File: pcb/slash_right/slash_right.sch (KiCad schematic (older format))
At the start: 138 parts, among them J1 RJ12, J2 AVR-ISP-6, J3 USB_B_Mini, SW1 SW_Push, SW10 SW_Push_45deg, SW11 SW_Push_45deg, SW12 SW_Push_45deg, SW13 SW_Push_45deg, SW14 SW_Push_45deg, SW15 SW_Push_45deg, SW16 SW_Push_45deg, SW17 SW_Push_45deg, SW18 SW_Push_45deg, SW19 SW_Push_45deg, SW2 SW_Push_45deg, SW20 SW_Push_45deg, SW21 SW_Push_45deg, SW22 SW_Push_45deg, SW23 SW_Push_45deg, SW24 SW_Push_45deg, SW25 SW_Push_45deg, SW26 SW_Push_45deg, SW27 SW_Push_45deg, SW28 SW_Push_45deg, SW29 SW_Push_45deg, SW3 SW_Push_45deg, SW30 SW_Push_45deg, SW31 SW_Push_45deg, SW32 SW_Push_45deg, SW33 SW_Push_45deg, SW34 SW_Push_45deg, SW35 SW_Push_45deg, SW36 SW_Push_45deg, SW37 SW_Push_45deg, SW38 SW_Push_45deg, SW39 SW_Push_45deg, SW4 SW_Push_45deg, SW40 SW_Push_45deg, SW41 SW_Push_45deg, SW42 SW_Push_45deg, SW43 SW_Push_45deg, SW44 SW_Push_45deg, SW45 SW_Push_45deg, SW46 SW_Push_45deg, SW47 SW_Push_45deg, SW48 SW_Push_45deg, SW49 SW_Push_45deg, SW5 SW_Push_45deg, SW50 SW_Push_45deg, SW51 SW_Push_45deg, SW52 SW_Push_45deg, SW53 SW_Push_45deg, SW54 SW_Push_45deg, SW55 SW_Push_45deg, SW56 SW_Push_45deg, SW6 SW_Push_45deg, SW7 SW_Push_45deg, SW8 SW_Push_45deg, SW9 SW_Push_45deg, U1 ATmega32U4-AU, Y1 16MHz

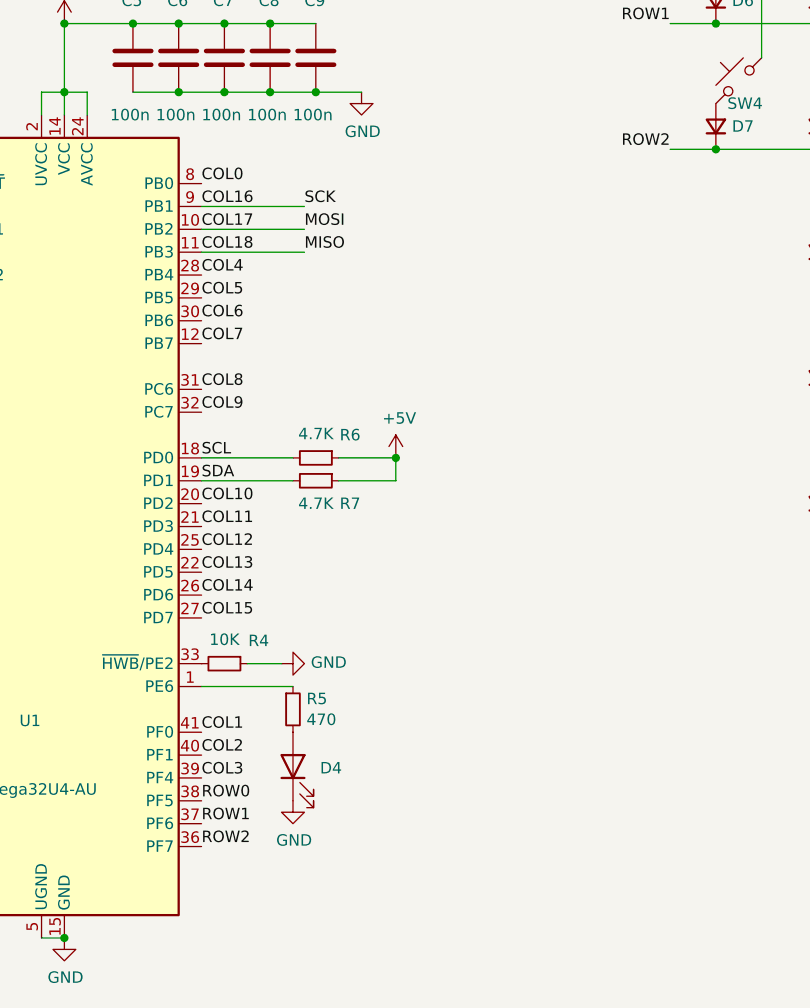
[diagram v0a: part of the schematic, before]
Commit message: pcb: slash: more routing
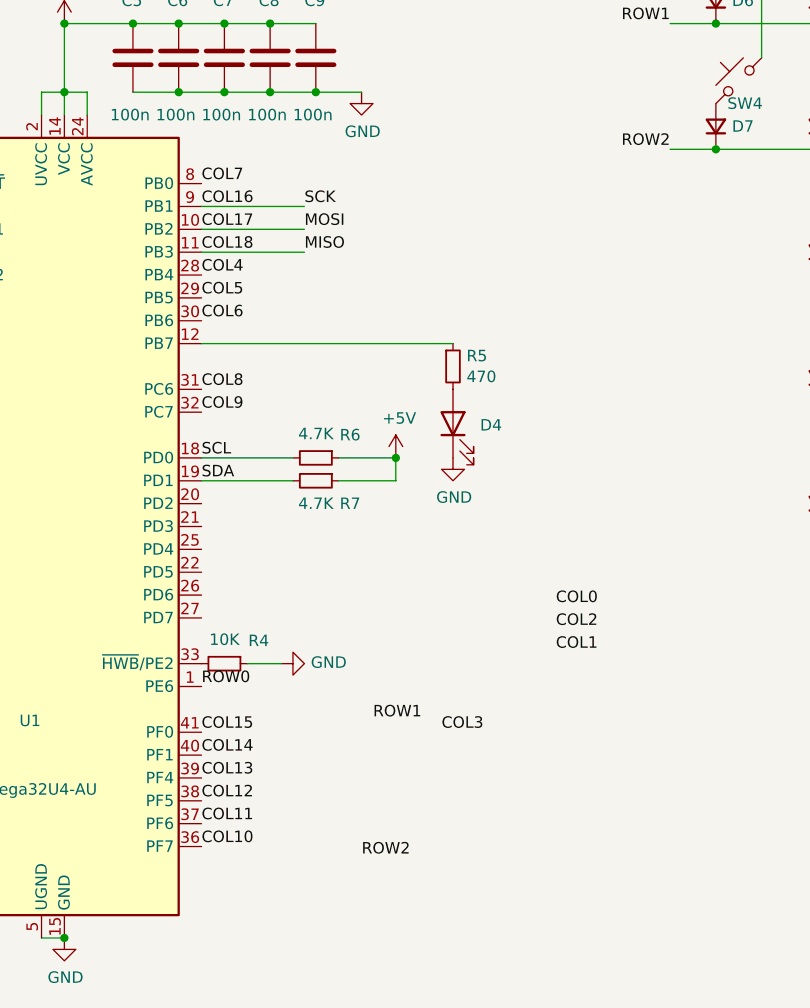
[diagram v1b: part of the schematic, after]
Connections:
- net COL0: no longer U1.8 (PB0)
- net COL1: no longer U1.41 (PF0)
- net COL10: now also U1.36 (PF7); no longer U1.20 (PD2)
- net COL11: now also U1.37 (PF6); no longer U1.21 (PD3)
- net COL12: now also U1.38 (PF5); no longer U1.25 (PD4)
- net COL13: now also U1.39 (PF4); no longer U1.22 (PD5)
- net COL14: now also U1.40 (PF1); no longer U1.26 (PD6)
- net COL15: now also U1.41 (PF0); no longer U1.27 (PD7)
- net COL2: no longer U1.40 (PF1)
- net COL3: no longer U1.39 (PF4)
- net COL7: now also U1.8 (PB0); no longer U1.12 (PB7)
- net ROW0: now also U1.1 (PE6); no longer U1.38 (PF5)
- net ROW1: no longer U1.37 (PF6)
- net ROW2: no longer U1.36 (PF7)
- net at R5.1: now also U1.12 (PB7); no longer U1.1 (PE6)
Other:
- moved on the sheet: D4, R5
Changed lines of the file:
@@
 Text Label 1300 3500 0    50   ~ 0
 ~RST
-Wire Wire Line
-	4100 5900 4500 5900
 $Comp
 L Device:R_Small R5
 U 1 1 616328C2
-P 4500 6000
-F 0 "R5" H 4559 6046 50  0000 L CNN
-F 1 "470" H 4559 5955 50  0000 L CNN
-F 2 "Resistor_SMD:R_0805_2012Metric_Pad1.20x1.40mm_HandSolder" H 4500 6000 50  0001 C CNN
-F 3 "~" H 4500 6000 50  0001 C CNN
-	1    4500 6000
+P 5200 4500
+F 0 "R5" H 5259 4546 50  0000 L CNN
+F 1 "470" H 5259 4455 50  0000 L CNN
+F 2 "Resistor_SMD:R_0805_2012Metric_Pad1.20x1.40mm_HandSolder" H 5200 4500 50  0001 C CNN
+F 3 "~" H 5200 4500 50  0001 C CNN
+	1    5200 4500
 	1    0    0    -1
 $EndComp
@@
 L Device:LED D4
 U 1 1 61633622
-P 4500 6250
-F 0 "D4" V 4493 6132 50  0000 R CNN
-F 1 "LED" V 4448 6132 50  0001 R CNN
-F 2 "LED_SMD:LED_0805_2012Metric_Pad1.15x1.40mm_HandSolder" H 4500 6250 50  0001 C CNN
-F 3 "~" H 4500 6250 50  0001 C CNN
-	1    4500 6250
+P 5200 4750
+F 0 "D4" V 5193 4632 50  0000 R CNN
+F 1 "LED" V 5148 4632 50  0001 R CNN
+F 2 "LED_SMD:LED_0805_2012Metric_Pad1.15x1.40mm_HandSolder" H 5200 4750 50  0001 C CNN
+F 3 "~" H 5200 4750 50  0001 C CNN
+	1    5200 4750
 	0    -1   -1   0
 $EndComp
@@
 L power:GND #PWR020
 U 1 1 616340EE
-P 4500 6400
-F 0 "#PWR020" H 4500 6150 50  0001 C CNN
-F 1 "GND" H 4505 6227 50  0000 C CNN
-F 2 "" H 4500 6400 50  0001 C CNN
-F 3 "" H 4500 6400 50  0001 C CNN
-	1    4500 6400
+P 5200 4900
+F 0 "#PWR020" H 5200 4650 50  0001 C CNN
+F 1 "GND" H 5205 4727 50  0000 C CNN
+F 2 "" H 5200 4900 50  0001 C CNN
+F 3 "" H 5200 4900 50  0001 C CNN
+	1    5200 4900
 	1    0    0    -1
 $EndComp
@@
 Wire Wire Line
 	4100 4000 4550 4000
-Text Label 4100 3700 0    50   ~ 0
+Text Label 5650 5550 0    50   ~ 0
 COL0
-Text Label 4100 6100 0    50   ~ 0
+Text Label 5650 5750 0    50   ~ 0
 COL1
-Text Label 4100 6200 0    50   ~ 0
+Text Label 5650 5650 0    50   ~ 0
 COL2
-Text Label 4100 6300 0    50   ~ 0
+Text Label 5150 6100 0    50   ~ 0
 COL3
 Text Label 4100 4100 0    50   ~ 0
@@
 Text Label 4100 4300 0    50   ~ 0
 COL6
-Text Label 4100 4400 0    50   ~ 0
+Text Label 4100 3700 0    50   ~ 0
 COL7
 Text Label 4100 4600 0    50   ~ 0
@@
 Text Label 4100 4700 0    50   ~ 0
 COL9
-Text Label 4100 5100 0    50   ~ 0
+Text Label 4100 6600 0    50   ~ 0
 COL10
 Text Label 7450 5500 3    50   ~ 0
 COL11
-Text Label 4100 5200 0    50   ~ 0
+Text Label 4100 6500 0    50   ~ 0
 COL11
-Text Label 4100 5300 0    50   ~ 0
+Text Label 4100 6400 0    50   ~ 0
 COL12
-Text Label 4100 5400 0    50   ~ 0
+Text Label 4100 6300 0    50   ~ 0
 COL13
-Text Label 4100 5500 0    50   ~ 0
+Text Label 4100 6200 0    50   ~ 0
 COL14
-Text Label 4100 5600 0    50   ~ 0
+Text Label 4100 6100 0    50   ~ 0
 COL15
 Connection ~ 10150 4250
@@
 	0    -1   -1   0
 $EndComp
-Text Label 4100 6400 0    50   ~ 0
+Text Label 4100 5900 0    50   ~ 0
 ROW0
-Text Label 4100 6500 0    50   ~ 0
+Text Label 4850 6050 0    50   ~ 0
 ROW1
-Text Label 4100 6600 0    50   ~ 0
+Text Label 4800 6650 0    50   ~ 0
 ROW2
 $Comp
@@
 Text Label 4100 4000 0    50   ~ 0
 COL18
+Wire Wire Line
+	5200 4400 4100 4400
 $EndSCHEMATC

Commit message: pcb: slash: right: Finish routing
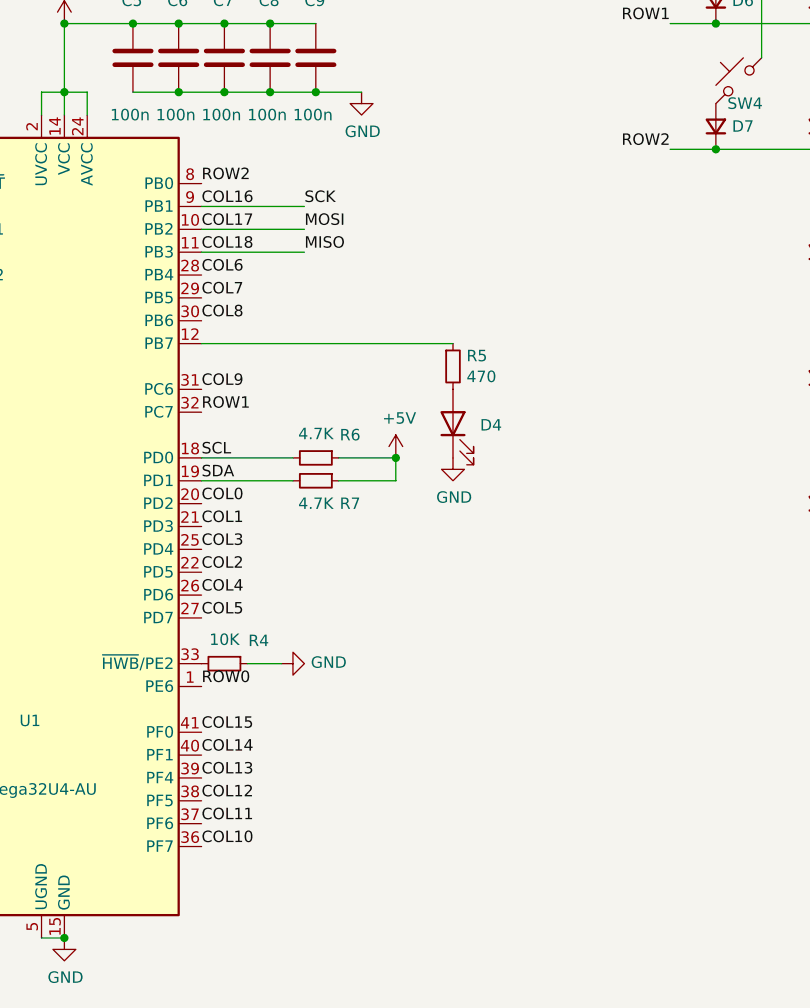
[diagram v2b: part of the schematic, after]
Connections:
- net COL0: now also U1.20 (PD2)
- net COL1: now also U1.21 (PD3)
- net COL2: now also U1.22 (PD5)
- net COL3: now also U1.25 (PD4)
- net COL4: now also U1.26 (PD6); no longer U1.28 (PB4)
- net COL5: now also U1.27 (PD7); no longer U1.29 (PB5)
- net COL6: now also U1.28 (PB4); no longer U1.30 (PB6)
- net COL7: now also U1.29 (PB5); no longer U1.8 (PB0)
- net COL8: now also U1.30 (PB6); no longer U1.31 (PC6)
- net COL9: now also U1.31 (PC6); no longer U1.32 (PC7)
- net ROW1: now also U1.32 (PC7)
- net ROW2: now also U1.8 (PB0)
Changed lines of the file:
@@
 Wire Wire Line
 	4100 4000 4550 4000
-Text Label 5650 5550 0    50   ~ 0
+Text Label 4100 5100 0    50   ~ 0
 COL0
-Text Label 5650 5750 0    50   ~ 0
+Text Label 4100 5200 0    50   ~ 0
 COL1
-Text Label 5650 5650 0    50   ~ 0
+Text Label 4100 5400 0    50   ~ 0
 COL2
-Text Label 5150 6100 0    50   ~ 0
+Text Label 4100 5300 0    50   ~ 0
 COL3
+Text Label 4100 5500 0    50   ~ 0
+COL4
+Text Label 4100 5600 0    50   ~ 0
+COL5
 Text Label 4100 4100 0    50   ~ 0
-COL4
+COL6
 Text Label 4100 4200 0    50   ~ 0
-COL5
+COL7
 Text Label 4100 4300 0    50   ~ 0
-COL6
-Text Label 4100 3700 0    50   ~ 0
-COL7
+COL8
 Text Label 4100 4600 0    50   ~ 0
-COL8
-Text Label 4100 4700 0    50   ~ 0
 COL9
 Text Label 4100 6600 0    50   ~ 0
@@
 Text Label 4100 5900 0    50   ~ 0
 ROW0
-Text Label 4850 6050 0    50   ~ 0
+Text Label 4100 4700 0    50   ~ 0
 ROW1
-Text Label 4800 6650 0    50   ~ 0
+Text Label 4100 3700 0    50   ~ 0
 ROW2
 $Comp
